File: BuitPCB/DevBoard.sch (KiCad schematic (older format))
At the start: 1 part, among them U1 Teensy4.1

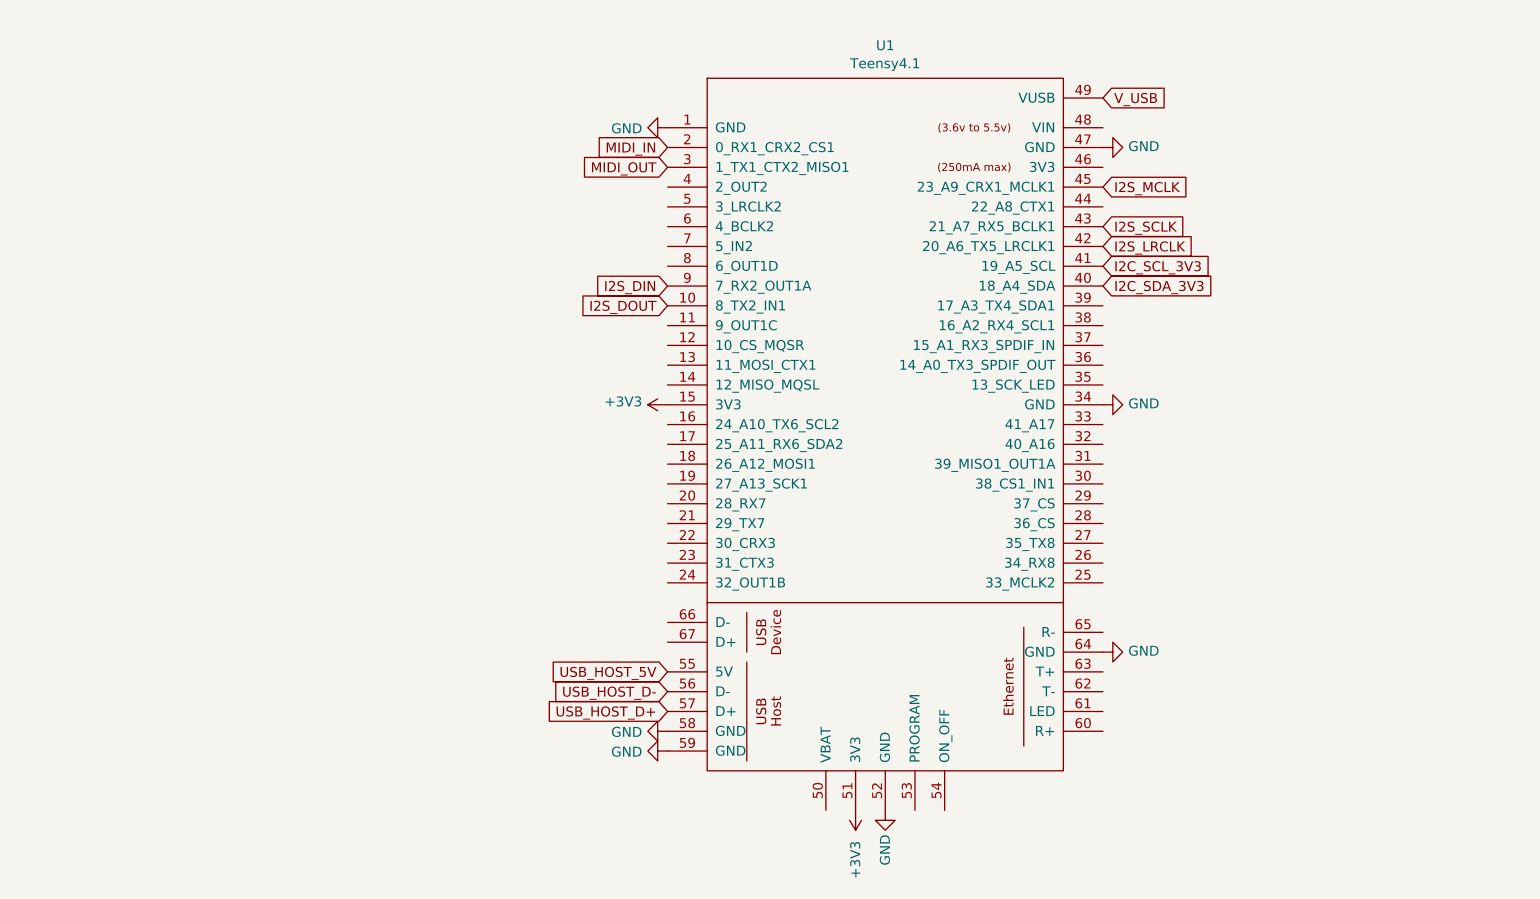
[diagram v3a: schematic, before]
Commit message: Updated adding esp8266 transceiver module
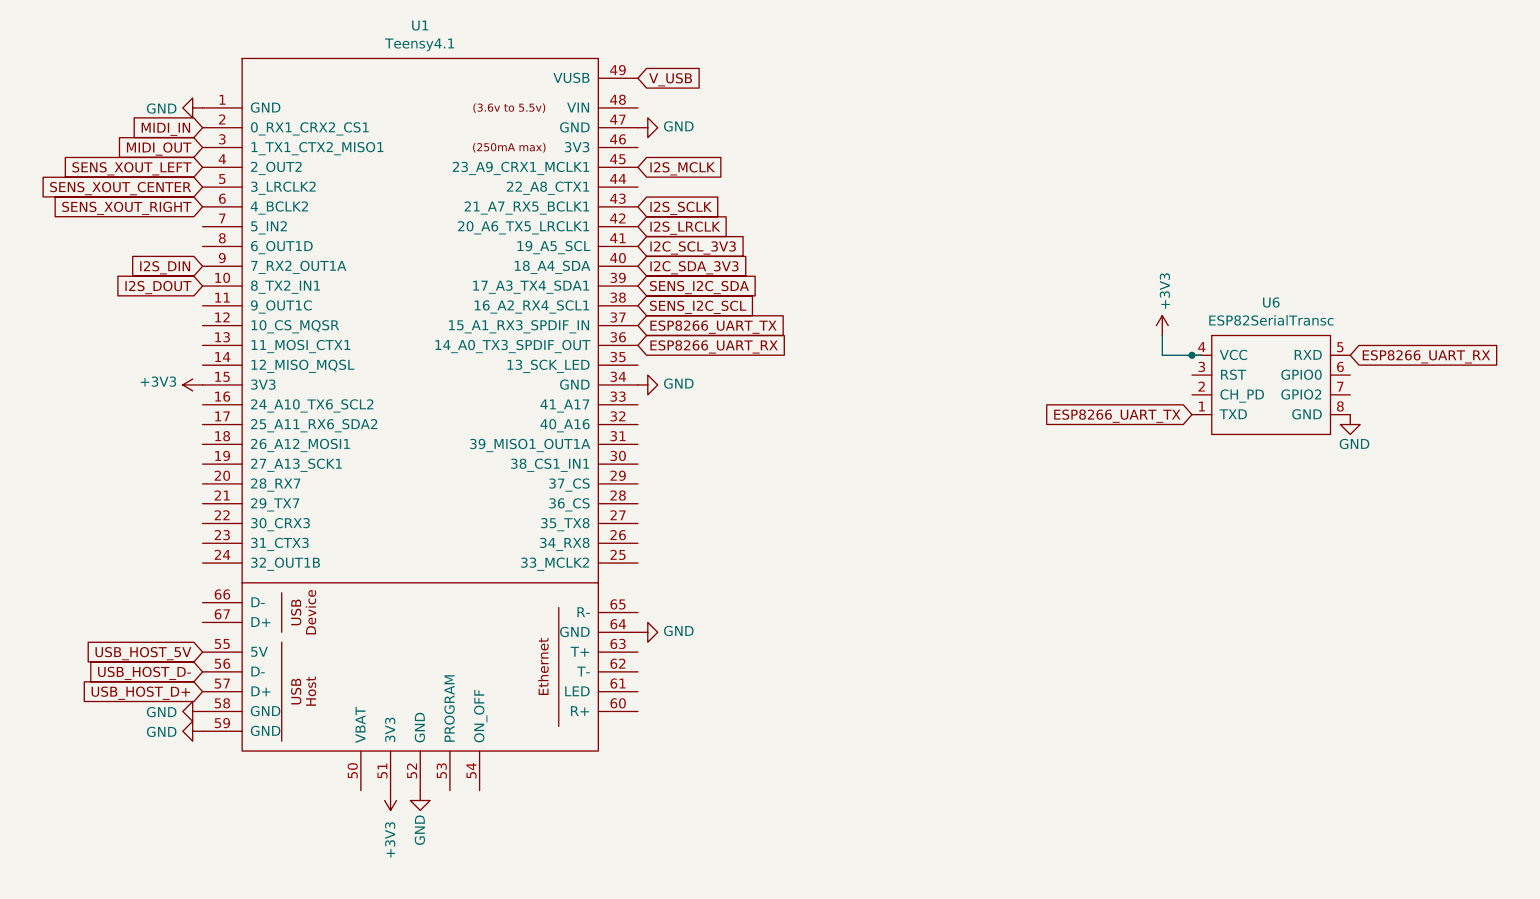
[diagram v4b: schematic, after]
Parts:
- added U6: ESP82SerialTransc, ESP32-Footprints:ESP82SerialTransceiver, symbol RTPLibs:ESP82SerialTransc
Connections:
- net labels added: ESP8266_UART_RX, ESP8266_UART_TX, SENS_I2C_SCL, SENS_I2C_SDA, SENS_XOUT_CENTER, SENS_XOUT_LEFT, SENS_XOUT_RIGHT
- wire segments 0 -> 3
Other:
- moved on the sheet: U1
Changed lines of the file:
@@
 L teensy:Teensy4.1 U?
 U 1 1 61A96076
-P 6050 4000
+P 3700 3900
 AR Path="/61A96076" Ref="U?"  Part="1"
 AR Path="/61A90B8E/61A96076" Ref="U1"  Part="1"
-F 0 "U1" H 6050 6565 50  0000 C CNN
-F 1 "Teensy4.1" H 6050 6474 50  0000 C CNN
-F 2 "teensy:Teensy41" H 5650 4400 50  0001 C CNN
-F 3 "" H 5650 4400 50  0001 C CNN
-	1    6050 4000
+F 0 "U1" H 3700 6465 50  0000 C CNN
+F 1 "Teensy4.1" H 3700 6374 50  0000 C CNN
+F 2 "teensy:Teensy41" H 3300 4300 50  0001 C CNN
+F 3 "" H 3300 4300 50  0001 C CNN
+	1    3700 3900
 	1    0    0    -1
 $EndComp
@@
 L power:GND #PWR0101
 U 1 1 61A9C991
-P 4950 1850
-F 0 "#PWR0101" H 4950 1600 50  0001 C CNN
-F 1 "GND" V 4955 1722 50  0000 R CNN
-F 2 "" H 4950 1850 50  0001 C CNN
-F 3 "" H 4950 1850 50  0001 C CNN
-	1    4950 1850
+P 2600 1750
+F 0 "#PWR0101" H 2600 1500 50  0001 C CNN
+F 1 "GND" V 2605 1622 50  0000 R CNN
+F 2 "" H 2600 1750 50  0001 C CNN
+F 3 "" H 2600 1750 50  0001 C CNN
+	1    2600 1750
 	0    1    1    0
 $EndComp
@@
 L power:GND #PWR0102
 U 1 1 61A9CF3F
-P 6050 5300
-F 0 "#PWR0102" H 6050 5050 50  0001 C CNN
-F 1 "GND" V 6050 5100 50  0000 C CNN
-F 2 "" H 6050 5300 50  0001 C CNN
-F 3 "" H 6050 5300 50  0001 C CNN
-	1    6050 5300
+P 3700 5200
+F 0 "#PWR0102" H 3700 4950 50  0001 C CNN
+F 1 "GND" V 3700 5000 50  0000 C CNN
+F 2 "" H 3700 5200 50  0001 C CNN
+F 3 "" H 3700 5200 50  0001 C CNN
+	1    3700 5200
 	1    0    0    -1
 $EndComp
@@
 L power:GND #PWR0103
 U 1 1 61A9EF5C
-P 4950 4900
-F 0 "#PWR0103" H 4950 4650 50  0001 C CNN
-F 1 "GND" V 4955 4772 50  0000 R CNN
-F 2 "" H 4950 4900 50  0001 C CNN
-F 3 "" H 4950 4900 50  0001 C CNN
-	1    4950 4900
+P 2600 4800
+F 0 "#PWR0103" H 2600 4550 50  0001 C CNN
+F 1 "GND" V 2605 4672 50  0000 R CNN
+F 2 "" H 2600 4800 50  0001 C CNN
+F 3 "" H 2600 4800 50  0001 C CNN
+	1    2600 4800
 	0    1    1    0
 $EndComp
@@
 L power:GND #PWR0104
 U 1 1 61A9F9EA
-P 4950 5000
-F 0 "#PWR0104" H 4950 4750 50  0001 C CNN
-F 1 "GND" V 4955 4872 50  0000 R CNN
-F 2 "" H 4950 5000 50  0001 C CNN
-F 3 "" H 4950 5000 50  0001 C CNN
-	1    4950 5000
+P 2600 4900
+F 0 "#PWR0104" H 2600 4650 50  0001 C CNN
+F 1 "GND" V 2605 4772 50  0000 R CNN
+F 2 "" H 2600 4900 50  0001 C CNN
+F 3 "" H 2600 4900 50  0001 C CNN
+	1    2600 4900
 	0    1    1    0
 $EndComp
@@
 L power:GND #PWR0105
 U 1 1 61A9FFE0
-P 7150 3250
-F 0 "#PWR0105" H 7150 3000 50  0001 C CNN
-F 1 "GND" V 7155 3122 50  0000 R CNN
-F 2 "" H 7150 3250 50  0001 C CNN
-F 3 "" H 7150 3250 50  0001 C CNN
-	1    7150 3250
+P 4800 3150
+F 0 "#PWR0105" H 4800 2900 50  0001 C CNN
+F 1 "GND" V 4805 3022 50  0000 R CNN
+F 2 "" H 4800 3150 50  0001 C CNN
+F 3 "" H 4800 3150 50  0001 C CNN
+	1    4800 3150
 	0    -1   -1   0
 $EndComp
@@
 L power:GND #PWR0106
 U 1 1 61AA08C4
-P 7150 1950
-F 0 "#PWR0106" H 7150 1700 50  0001 C CNN
-F 1 "GND" V 7155 1822 50  0000 R CNN
-F 2 "" H 7150 1950 50  0001 C CNN
-F 3 "" H 7150 1950 50  0001 C CNN
-	1    7150 1950
+P 4800 1850
+F 0 "#PWR0106" H 4800 1600 50  0001 C CNN
+F 1 "GND" V 4805 1722 50  0000 R CNN
+F 2 "" H 4800 1850 50  0001 C CNN
+F 3 "" H 4800 1850 50  0001 C CNN
+	1    4800 1850
 	0    -1   -1   0
 $EndComp
@@
 L power:GND #PWR0107
 U 1 1 61AA1181
-P 7150 4500
-F 0 "#PWR0107" H 7150 4250 50  0001 C CNN
-F 1 "GND" V 7155 4372 50  0000 R CNN
-F 2 "" H 7150 4500 50  0001 C CNN
-F 3 "" H 7150 4500 50  0001 C CNN
-	1    7150 4500
+P 4800 4400
+F 0 "#PWR0107" H 4800 4150 50  0001 C CNN
+F 1 "GND" V 4805 4272 50  0000 R CNN
+F 2 "" H 4800 4400 50  0001 C CNN
+F 3 "" H 4800 4400 50  0001 C CNN
+	1    4800 4400
 	0    -1   -1   0
 $EndComp
-Text GLabel 4950 4800 0    50   Input ~ 0
+Text GLabel 2600 4700 0    50   Input ~ 0
 USB_HOST_D+
-Text GLabel 4950 4700 0    50   Input ~ 0
+Text GLabel 2600 4600 0    50   Input ~ 0
 USB_HOST_D-
 $Comp
 L power:+3V3 #PWR0108
 U 1 1 61AB5F49
-P 4950 3250
-F 0 "#PWR0108" H 4950 3100 50  0001 C CNN
-F 1 "+3V3" V 4965 3378 50  0000 L CNN
-F 2 "" H 4950 3250 50  0001 C CNN
-F 3 "" H 4950 3250 50  0001 C CNN
-	1    4950 3250
+P 2600 3150
+F 0 "#PWR0108" H 2600 3000 50  0001 C CNN
+F 1 "+3V3" V 2615 3278 50  0000 L CNN
+F 2 "" H 2600 3150 50  0001 C CNN
+F 3 "" H 2600 3150 50  0001 C CNN
+	1    2600 3150
 	0    -1   -1   0
 $EndComp
@@
 L power:+3V3 #PWR0109
 U 1 1 61AB6DCC
-P 5900 5300
-F 0 "#PWR0109" H 5900 5150 50  0001 C CNN
-F 1 "+3V3" V 5900 5550 50  0000 C CNN
-F 2 "" H 5900 5300 50  0001 C CNN
-F 3 "" H 5900 5300 50  0001 C CNN
-	1    5900 5300
+P 3550 5200
+F 0 "#PWR0109" H 3550 5050 50  0001 C CNN
+F 1 "+3V3" V 3550 5450 50  0000 C CNN
+F 2 "" H 3550 5200 50  0001 C CNN
+F 3 "" H 3550 5200 50  0001 C CNN
+	1    3550 5200
 	-1   0    0    1
 $EndComp
-Text GLabel 4950 4600 0    50   Input ~ 0
+Text GLabel 2600 4500 0    50   Input ~ 0
 USB_HOST_5V
-Text GLabel 7150 2650 2    50   Input ~ 0
+Text GLabel 4800 2550 2    50   Input ~ 0
 I2C_SDA_3V3
-Text GLabel 7150 2550 2    50   Input ~ 0
+Text GLabel 4800 2450 2    50   Input ~ 0
 I2C_SCL_3V3
-Text GLabel 7150 2150 2    50   Input ~ 0
+Text GLabel 4800 2050 2    50   Input ~ 0
 I2S_MCLK
-Text GLabel 7150 2450 2    50   Input ~ 0
+Text GLabel 4800 2350 2    50   Input ~ 0
 I2S_LRCLK
-Text GLabel 4950 2750 0    50   Input ~ 0
+Text GLabel 2600 2650 0    50   Input ~ 0
 I2S_DOUT
-Text GLabel 4950 2650 0    50   Input ~ 0
+Text GLabel 2600 2550 0    50   Input ~ 0
 I2S_DIN
-Text GLabel 7150 2350 2    50   Input ~ 0
+Text GLabel 4800 2250 2    50   Input ~ 0
 I2S_SCLK
-Text GLabel 4950 1950 0    50   Input ~ 0
+Text GLabel 2600 1850 0    50   Input ~ 0
 MIDI_IN
-Text GLabel 4950 2050 0    50   Input ~ 0
+Text GLabel 2600 1950 0    50   Input ~ 0
 MIDI_OUT
-Text GLabel 7150 1700 2    50   Input ~ 0
+Text GLabel 4800 1600 2    50   Input ~ 0
 V_USB
+$Comp
+L RTPLibs:ESP82SerialTransc U6
+U 1 1 61BDB2A6
+P 8000 3150
+F 0 "U6" H 8000 3565 50  0000 C CNN
+F 1 "ESP82SerialTransc" H 8000 3474 50  0000 C CNN
+F 2 "ESP32-Footprints:ESP82SerialTransceiver" H 7600 3600 50  0001 C CNN
+F 3 "" H 7600 3600 50  0001 C CNN
+	1    8000 3150
+	1    0    0    -1
+$EndComp
+$Comp
+L power:+3V3 #PWR032
+U 1 1 61BDB9FF
+P 7450 2900
+F 0 "#PWR032" H 7450 2750 50  0001 C CNN
+F 1 "+3V3" V 7465 3028 50  0000 L CNN
+F 2 "" H 7450 2900 50  0001 C CNN
+F 3 "" H 7450 2900 50  0001 C CNN
+	1    7450 2900
+	1    0    0    -1
+$EndComp
+$Comp
+L power:GND #PWR033
+U 1 1 61BDC76E
+P 8400 3300
+F 0 "#PWR033" H 8400 3050 50  0001 C CNN
+F 1 "GND" H 8500 3150 50  0000 R CNN
+F 2 "" H 8400 3300 50  0001 C CNN
+F 3 "" H 8400 3300 50  0001 C CNN
+	1    8400 3300
+	1    0    0    -1
+$EndComp
+Wire Wire Line
+	7650 3000 7600 3000
+Wire Wire Line
+	7450 3000 7450 2900
+Connection ~ 7600 3000
+Wire Wire Line
+	7600 3000 7450 3000
+Text GLabel 8400 3000 2    50   Input ~ 0
+ESP8266_UART_RX
+Text GLabel 7600 3300 0    50   Input ~ 0
+ESP8266_UART_TX
+Text GLabel 4800 2850 2    50   Input ~ 0
+ESP8266_UART_TX
+Text GLabel 4800 2950 2    50   Input ~ 0
+ESP8266_UART_RX
+Text GLabel 4800 2750 2    50   Input ~ 0
+SENS_I2C_SCL
+Text GLabel 4800 2650 2    50   Input ~ 0
+SENS_I2C_SDA
+Text GLabel 2600 2050 0    50   Input ~ 0
+SENS_XOUT_LEFT
+Text GLabel 2600 2150 0    50   Input ~ 0
+SENS_XOUT_CENTER
+Text GLabel 2600 2250 0    50   Input ~ 0
+SENS_XOUT_RIGHT
 $EndSCHEMATC

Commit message: Updated to almost every component and started routing
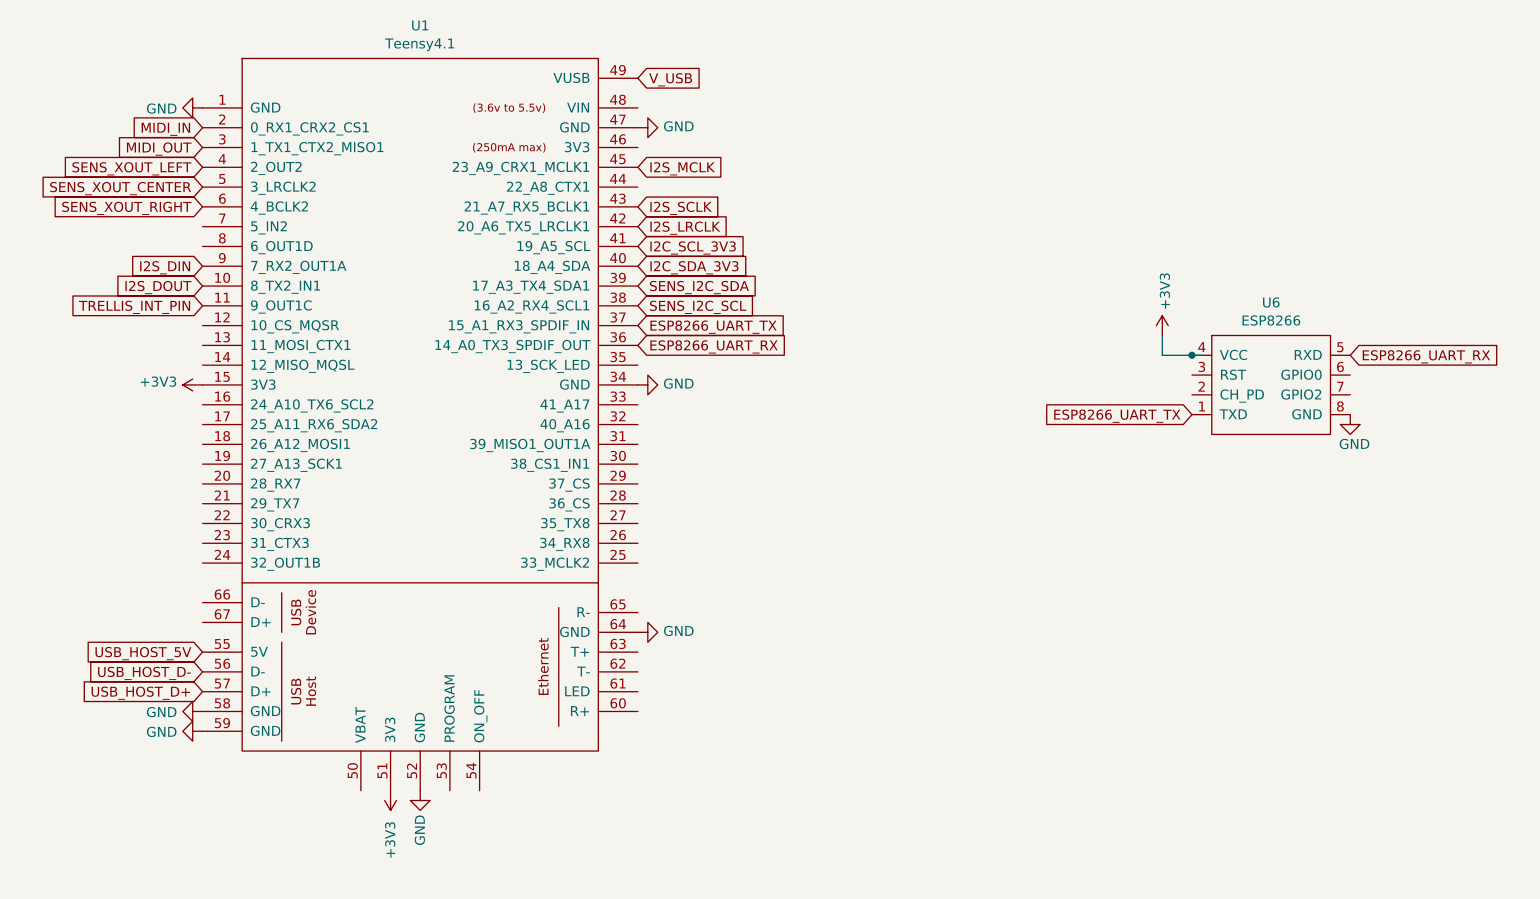
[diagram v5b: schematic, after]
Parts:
- U6: value ESP82SerialTransc -> ESP8266
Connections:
- net labels added: TRELLIS_INT_PIN
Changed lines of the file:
@@
 P 8000 3150
 F 0 "U6" H 8000 3565 50  0000 C CNN
-F 1 "ESP82SerialTransc" H 8000 3474 50  0000 C CNN
+F 1 "ESP8266" H 8000 3474 50  0000 C CNN
 F 2 "ESP32-Footprints:ESP82SerialTransceiver" H 7600 3600 50  0001 C CNN
 F 3 "" H 7600 3600 50  0001 C CNN
@@
 Text GLabel 2600 2250 0    50   Input ~ 0
 SENS_XOUT_RIGHT
+Text GLabel 2600 2750 0    50   Input ~ 0
+TRELLIS_INT_PIN
 $EndSCHEMATC
